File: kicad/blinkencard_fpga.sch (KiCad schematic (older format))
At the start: 19 parts, among them U1 ICE40UP5K-SG48ITR, U2 W25Q64JV

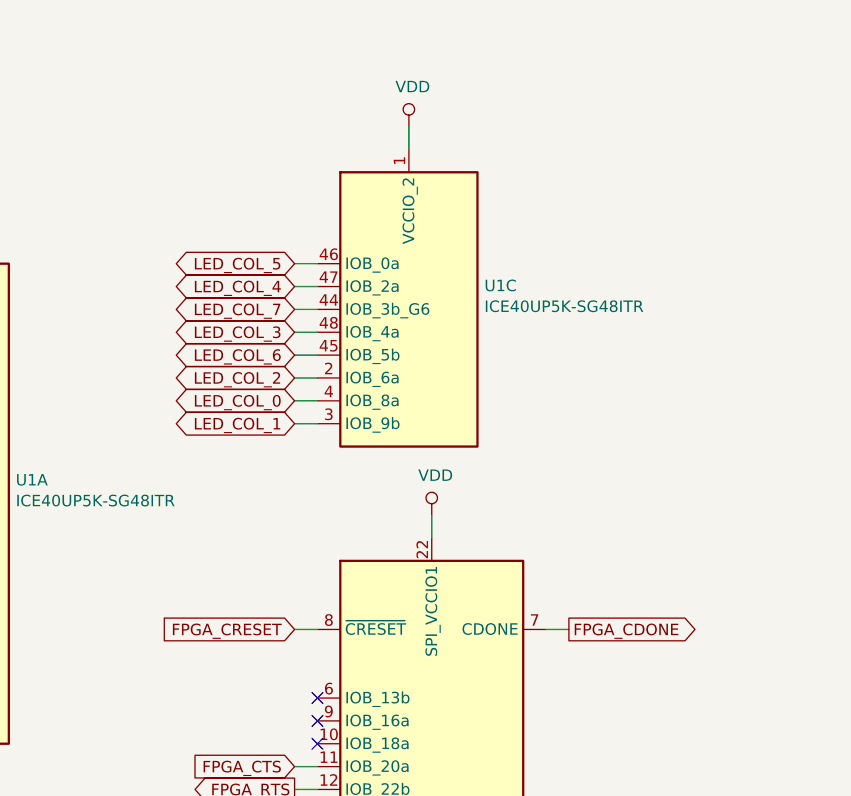
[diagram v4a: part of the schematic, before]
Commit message: Routing complete. DRC passes. Need to fix silk around LEDs and do final check
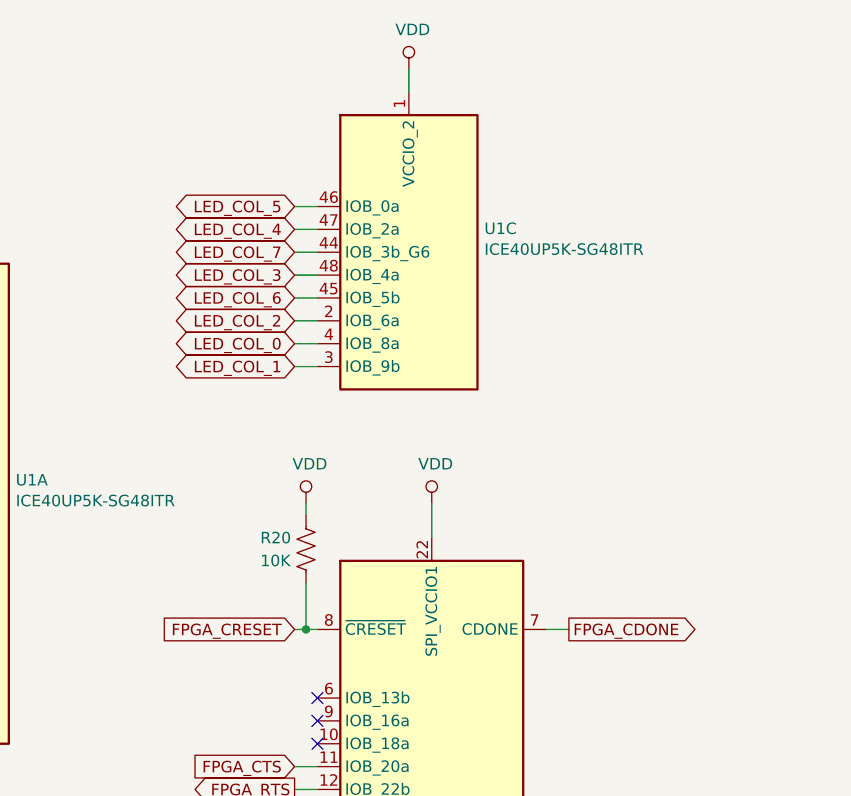
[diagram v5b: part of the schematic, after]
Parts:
- added R20: 10K, Resistor_SMD:R_0603_1608Metric, symbol Device:R_US
- U1: footprint Package_DFN_QFN:QFN-48-1EP_7x7mm_P0.5mm_EP5.6x5.6mm -> Package_DFN_QFN:QFN-48-1EP_7x7mm_P0.5mm_EP5.6x5.6mm_ThermalVias
- U2: footprint Package_SO:SOIC-8_5.23x5.23mm_P1.27mm -> Package_SO:SOIC-8_5.275x5.275mm_P1.27mm
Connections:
- net FPGA_CRESET: now also R20.2
- net VDD: now also R20.1
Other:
- moved on the sheet: U1C
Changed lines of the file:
@@
 F 0 "U1" H 5550 2825 50  0000 C CNN
 F 1 "ICE40UP5K-SG48ITR" H 5550 2734 50  0000 C CNN
-F 2 "Package_DFN_QFN:QFN-48-1EP_7x7mm_P0.5mm_EP5.6x5.6mm" H 5550 2550 50  0001 C CNN
+F 2 "Package_DFN_QFN:QFN-48-1EP_7x7mm_P0.5mm_EP5.6x5.6mm_ThermalVias" H 5550 2550 50  0001 C CNN
 F 3 "http://www.latticesemi.com/Products/FPGAandCPLD/iCE40Ultra" H 5150 4900 50  0001 C CNN
 	2    5550 3900
@@
 L FPGA_Lattice:ICE40UP5K-SG48ITR U1
 U 3 1 5DF0A464
-P 5450 1800
-F 0 "U1" H 5780 1903 50  0000 L CNN
-F 1 "ICE40UP5K-SG48ITR" H 5780 1812 50  0000 L CNN
-F 2 "Package_DFN_QFN:QFN-48-1EP_7x7mm_P0.5mm_EP5.6x5.6mm" H 5450 450 50  0001 C CNN
-F 3 "http://www.latticesemi.com/Products/FPGAandCPLD/iCE40Ultra" H 5050 2800 50  0001 C CNN
-	3    5450 1800
+P 5450 1550
+F 0 "U1" H 5780 1653 50  0000 L CNN
+F 1 "ICE40UP5K-SG48ITR" H 5780 1562 50  0000 L CNN
+F 2 "Package_DFN_QFN:QFN-48-1EP_7x7mm_P0.5mm_EP5.6x5.6mm_ThermalVias" H 5450 200 50  0001 C CNN
+F 3 "http://www.latticesemi.com/Products/FPGAandCPLD/iCE40Ultra" H 5050 2550 50  0001 C CNN
+	3    5450 1550
 	1    0    0    -1
 $EndComp
@@
 F 0 "U1" H 8680 2146 50  0000 L CNN
 F 1 "ICE40UP5K-SG48ITR" H 8680 2055 50  0000 L CNN
-F 2 "Package_DFN_QFN:QFN-48-1EP_7x7mm_P0.5mm_EP5.6x5.6mm" H 8450 750 50  0001 C CNN
+F 2 "Package_DFN_QFN:QFN-48-1EP_7x7mm_P0.5mm_EP5.6x5.6mm_ThermalVias" H 8450 750 50  0001 C CNN
 F 3 "http://www.latticesemi.com/Products/FPGAandCPLD/iCE40Ultra" H 8050 3100 50  0001 C CNN
 	4    8450 2100
@@
 Wire Wire Line
 	3000 3600 2900 3600
-Text GLabel 4950 2300 0    50   3State ~ 0
+Text GLabel 4950 2050 0    50   3State ~ 0
 LED_COL_1
-Text GLabel 4950 2200 0    50   3State ~ 0
+Text GLabel 4950 1950 0    50   3State ~ 0
 LED_COL_0
-Text GLabel 4950 2100 0    50   3State ~ 0
+Text GLabel 4950 1850 0    50   3State ~ 0
 LED_COL_2
-Text GLabel 4950 2000 0    50   3State ~ 0
+Text GLabel 4950 1750 0    50   3State ~ 0
 LED_COL_6
-Text GLabel 4950 1900 0    50   3State ~ 0
+Text GLabel 4950 1650 0    50   3State ~ 0
 LED_COL_3
-Text GLabel 4950 1800 0    50   3State ~ 0
+Text GLabel 4950 1550 0    50   3State ~ 0
 LED_COL_7
-Text GLabel 4950 1700 0    50   3State ~ 0
+Text GLabel 4950 1450 0    50   3State ~ 0
 LED_COL_4
-Text GLabel 4950 1600 0    50   3State ~ 0
+Text GLabel 4950 1350 0    50   3State ~ 0
 LED_COL_5
 Wire Wire Line
-	4950 1600 5050 1600
-Wire Wire Line
-	5050 1700 4950 1700
-Wire Wire Line
-	5050 1800 4950 1800
-Wire Wire Line
-	5050 1900 4950 1900
-Wire Wire Line
-	5050 2000 4950 2000
-Wire Wire Line
-	5050 2100 4950 2100
-Wire Wire Line
-	5050 2200 4950 2200
-Wire Wire Line
-	5050 2300 4950 2300
+	4950 1350 5050 1350
+Wire Wire Line
+	5050 1450 4950 1450
+Wire Wire Line
+	5050 1550 4950 1550
+Wire Wire Line
+	5050 1650 4950 1650
+Wire Wire Line
+	5050 1750 4950 1750
+Wire Wire Line
+	5050 1850 4950 1850
+Wire Wire Line
+	5050 1950 4950 1950
+Wire Wire Line
+	5050 2050 4950 2050
 Text GLabel 4950 4000 0    50   Output ~ 0
 FPGA_TXO
@@
 L power:VDD #PWR08
 U 1 1 5DF1A989
-P 5550 2700
-F 0 "#PWR08" H 5550 2550 50  0001 C CNN
-F 1 "VDD" H 5567 2873 50  0000 C CNN
-F 2 "" H 5550 2700 50  0001 C CNN
-F 3 "" H 5550 2700 50  0001 C CNN
-	1    5550 2700
+P 5550 2650
+F 0 "#PWR08" H 5550 2500 50  0001 C CNN
+F 1 "VDD" H 5567 2823 50  0000 C CNN
+F 2 "" H 5550 2650 50  0001 C CNN
+F 3 "" H 5550 2650 50  0001 C CNN
+	1    5550 2650
 	1    0    0    -1
 $EndComp
@@
 L power:VDD #PWR07
 U 1 1 5DF1B34D
-P 5450 1000
-F 0 "#PWR07" H 5450 850 50  0001 C CNN
-F 1 "VDD" H 5467 1173 50  0000 C CNN
-F 2 "" H 5450 1000 50  0001 C CNN
-F 3 "" H 5450 1000 50  0001 C CNN
-	1    5450 1000
+P 5450 750
+F 0 "#PWR07" H 5450 600 50  0001 C CNN
+F 1 "VDD" H 5467 923 50  0000 C CNN
+F 2 "" H 5450 750 50  0001 C CNN
+F 3 "" H 5450 750 50  0001 C CNN
+	1    5450 750
 	1    0    0    -1
 $EndComp
@@
 	3400 1400 3400 1500
 Wire Wire Line
-	5450 1000 5450 1100
-Wire Wire Line
-	5550 2700 5550 2800
+	5450 750  5450 850
 Text GLabel 2900 2000 0    50   Input ~ 0
 BUTTON_0
@@
 FPGA_CRESET
 Wire Wire Line
-	4950 3200 5050 3200
+	4950 3200 5000 3200
 Wire Wire Line
 	6050 3200 6150 3200
@@
 F 0 "U2" H 2750 6050 50  0000 C CNN
 F 1 "W25Q64JV" H 2850 5950 50  0000 C CNN
-F 2 "Package_SO:SOIC-8_5.23x5.23mm_P1.27mm" H 2450 5650 50  0001 C CNN
+F 2 "Package_SO:SOIC-8_5.275x5.275mm_P1.27mm" H 2450 5650 50  0001 C CNN
 F 3 "https://www.mouser.com/datasheet/2/949/w25q64jv_revj_03272018_plus-1489671.pdf" H 2450 5650 50  0001 C CNN
 	1    2450 5650
@@
 F 0 "U1" H 3730 2653 50  0000 L CNN
 F 1 "ICE40UP5K-SG48ITR" H 3730 2562 50  0000 L CNN
-F 2 "Package_DFN_QFN:QFN-48-1EP_7x7mm_P0.5mm_EP5.6x5.6mm" H 3400 1250 50  0001 C CNN
+F 2 "Package_DFN_QFN:QFN-48-1EP_7x7mm_P0.5mm_EP5.6x5.6mm_ThermalVias" H 3400 1250 50  0001 C CNN
 F 3 "http://www.latticesemi.com/Products/FPGAandCPLD/iCE40Ultra" H 3000 3600 50  0001 C CNN
 	1    3400 2600
@@
 	9950 4000 9450 4000
 Connection ~ 9450 4000
+$Comp
+L Device:R_US R20
+U 1 1 5DD19C71
+P 5000 2850
+F 0 "R20" H 4800 2900 50  0000 L CNN
+F 1 "10K" H 4800 2800 50  0000 L CNN
+F 2 "Resistor_SMD:R_0603_1608Metric" V 5040 2840 50  0001 C CNN
+F 3 "~" H 5000 2850 50  0001 C CNN
+	1    5000 2850
+	1    0    0    -1
+$EndComp
+Wire Wire Line
+	5000 3200 5000 3000
+Connection ~ 5000 3200
+Wire Wire Line
+	5000 3200 5050 3200
+$Comp
+L power:VDD #PWR023
+U 1 1 5DD2024B
+P 5000 2650
+F 0 "#PWR023" H 5000 2500 50  0001 C CNN
+F 1 "VDD" H 5017 2823 50  0000 C CNN
+F 2 "" H 5000 2650 50  0001 C CNN
+F 3 "" H 5000 2650 50  0001 C CNN
+	1    5000 2650
+	1    0    0    -1
+$EndComp
+Wire Wire Line
+	5000 2650 5000 2700
+Wire Wire Line
+	5550 2650 5550 2800
 $EndSCHEMATC

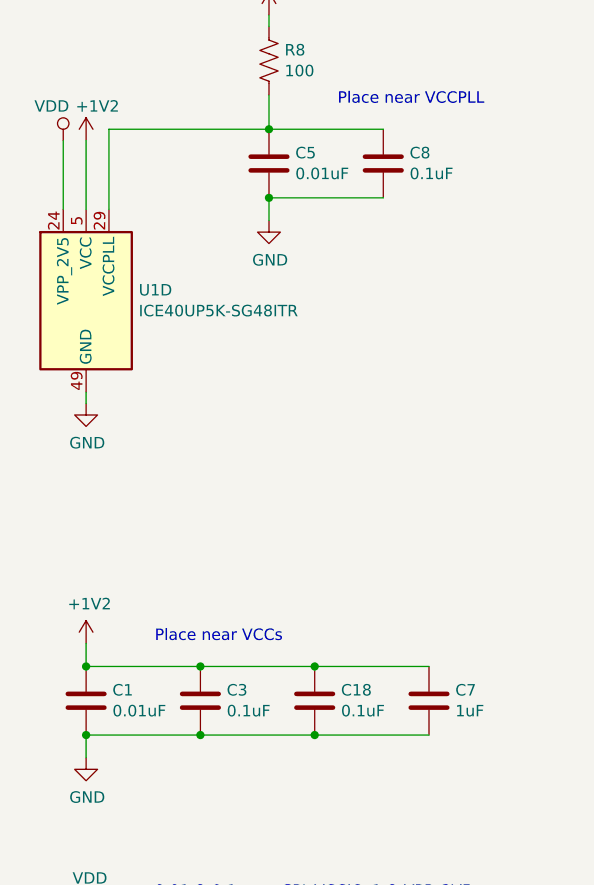
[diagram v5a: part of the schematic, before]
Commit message: Start v1.1 - minor fixes:
- Replace 4.7uF caps with 10uF
- Replace 0.01uF cap in the FPGA VCCPLL filter with 10uF per Lattice's design guideline
- All <1uF caps to 0603 sizes, 1-10uF to 0805
- Make TP? values match between schem and PCB
- Sanitize component values for BOM export consistency
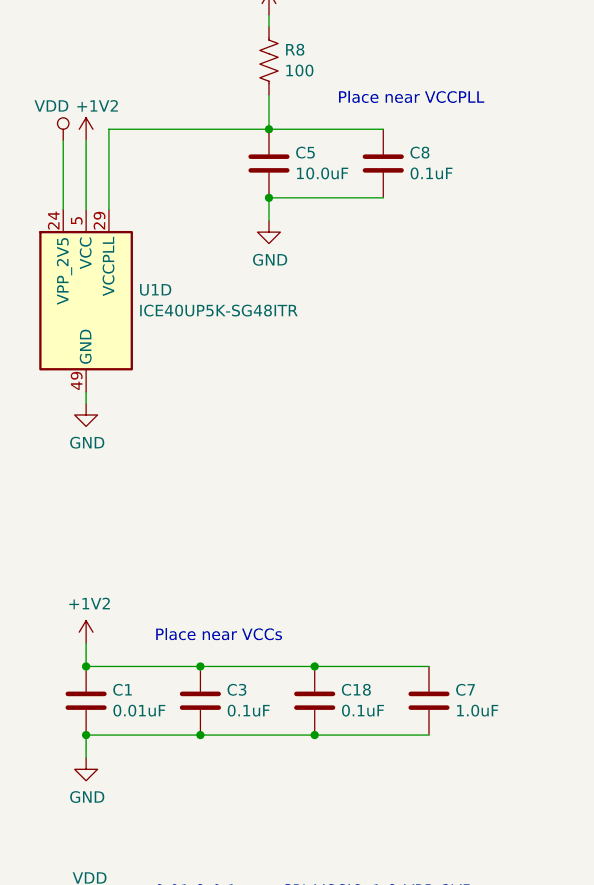
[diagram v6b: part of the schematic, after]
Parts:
- C1, C18, C2, C3, C4, C6, C8, C9: footprint Capacitor_SMD:C_0805_2012Metric -> Capacitor_SMD:C_0603_1608Metric
- C5: value 0.01uF -> 10.0uF
- C7: value 1uF -> 1.0uF
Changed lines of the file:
@@
 F 0 "C1" H 8565 3896 50  0000 L CNN
 F 1 "0.01uF" H 8565 3805 50  0000 L CNN
-F 2 "Capacitor_SMD:C_0805_2012Metric" H 8488 3700 50  0001 C CNN
+F 2 "Capacitor_SMD:C_0603_1608Metric" H 8488 3700 50  0001 C CNN
 F 3 "~" H 8450 3850 50  0001 C CNN
 	1    8450 3850
@@
 F 0 "C3" H 9065 3896 50  0000 L CNN
 F 1 "0.1uF" H 9065 3805 50  0000 L CNN
-F 2 "Capacitor_SMD:C_0805_2012Metric" H 8988 3700 50  0001 C CNN
+F 2 "Capacitor_SMD:C_0603_1608Metric" H 8988 3700 50  0001 C CNN
 F 3 "~" H 8950 3850 50  0001 C CNN
 	1    8950 3850
@@
 P 9950 3850
 F 0 "C7" H 10065 3896 50  0000 L CNN
-F 1 "1uF" H 10065 3805 50  0000 L CNN
+F 1 "1.0uF" H 10065 3805 50  0000 L CNN
 F 2 "Capacitor_SMD:C_0805_2012Metric" H 9988 3700 50  0001 C CNN
 F 3 "~" H 9950 3850 50  0001 C CNN
@@
 	1    0    0    -1
 $EndComp
-$Comp
-L Device:C C8
-U 1 1 5DD47433
-P 9750 1500
-F 0 "C8" H 9865 1546 50  0000 L CNN
-F 1 "0.1uF" H 9865 1455 50  0000 L CNN
-F 2 "Capacitor_SMD:C_0805_2012Metric" H 9788 1350 50  0001 C CNN
-F 3 "~" H 9750 1500 50  0001 C CNN
-	1    9750 1500
-	1    0    0    -1
-$EndComp
-$Comp
-L Device:C C5
-U 1 1 5DD47429
-P 9250 1500
-F 0 "C5" H 9365 1546 50  0000 L CNN
-F 1 "0.01uF" H 9365 1455 50  0000 L CNN
-F 2 "Capacitor_SMD:C_0805_2012Metric" H 9288 1350 50  0001 C CNN
-F 3 "~" H 9250 1500 50  0001 C CNN
-	1    9250 1500
-	1    0    0    -1
-$EndComp
 Wire Wire Line
 	8550 1700 8550 1350
@@
 F 0 "C2" H 8565 5096 50  0000 L CNN
 F 1 "0.01uF" H 8565 5005 50  0000 L CNN
-F 2 "Capacitor_SMD:C_0805_2012Metric" H 8488 4900 50  0001 C CNN
+F 2 "Capacitor_SMD:C_0603_1608Metric" H 8488 4900 50  0001 C CNN
 F 3 "~" H 8450 5050 50  0001 C CNN
 	1    8450 5050
@@
 F 0 "C4" H 9065 5096 50  0000 L CNN
 F 1 "0.1uF" H 9065 5005 50  0000 L CNN
-F 2 "Capacitor_SMD:C_0805_2012Metric" H 8988 4900 50  0001 C CNN
+F 2 "Capacitor_SMD:C_0603_1608Metric" H 8988 4900 50  0001 C CNN
 F 3 "~" H 8950 5050 50  0001 C CNN
 	1    8950 5050
@@
 F 0 "C9" H 10015 5096 50  0000 L CNN
 F 1 "0.1uF" H 10015 5005 50  0000 L CNN
-F 2 "Capacitor_SMD:C_0805_2012Metric" H 9938 4900 50  0001 C CNN
+F 2 "Capacitor_SMD:C_0603_1608Metric" H 9938 4900 50  0001 C CNN
 F 3 "~" H 9900 5050 50  0001 C CNN
 	1    9900 5050
@@
 F 0 "C6" H 9515 5096 50  0000 L CNN
 F 1 "0.1uF" H 9515 5005 50  0000 L CNN
-F 2 "Capacitor_SMD:C_0805_2012Metric" H 9438 4900 50  0001 C CNN
+F 2 "Capacitor_SMD:C_0603_1608Metric" H 9438 4900 50  0001 C CNN
 F 3 "~" H 9400 5050 50  0001 C CNN
 	1    9400 5050
@@
 F 0 "C18" H 9565 3896 50  0000 L CNN
 F 1 "0.1uF" H 9565 3805 50  0000 L CNN
-F 2 "Capacitor_SMD:C_0805_2012Metric" H 9488 3700 50  0001 C CNN
+F 2 "Capacitor_SMD:C_0603_1608Metric" H 9488 3700 50  0001 C CNN
 F 3 "~" H 9450 3850 50  0001 C CNN
 	1    9450 3850
@@
 Wire Wire Line
 	5550 2650 5550 2800
+$Comp
+L Device:C C8
+U 1 1 5DD47433
+P 9750 1500
+F 0 "C8" H 9865 1546 50  0000 L CNN
+F 1 "0.1uF" H 9865 1455 50  0000 L CNN
+F 2 "Capacitor_SMD:C_0603_1608Metric" H 9788 1350 50  0001 C CNN
+F 3 "~" H 9750 1500 50  0001 C CNN
+	1    9750 1500
+	1    0    0    -1
+$EndComp
+$Comp
+L Device:C C5
+U 1 1 5DD47429
+P 9250 1500
+F 0 "C5" H 9365 1546 50  0000 L CNN
+F 1 "10.0uF" H 9365 1455 50  0000 L CNN
+F 2 "Capacitor_SMD:C_0805_2012Metric" H 9288 1350 50  0001 C CNN
+F 3 "~" H 9250 1500 50  0001 C CNN
+	1    9250 1500
+	1    0    0    -1
+$EndComp
 $EndSCHEMATC

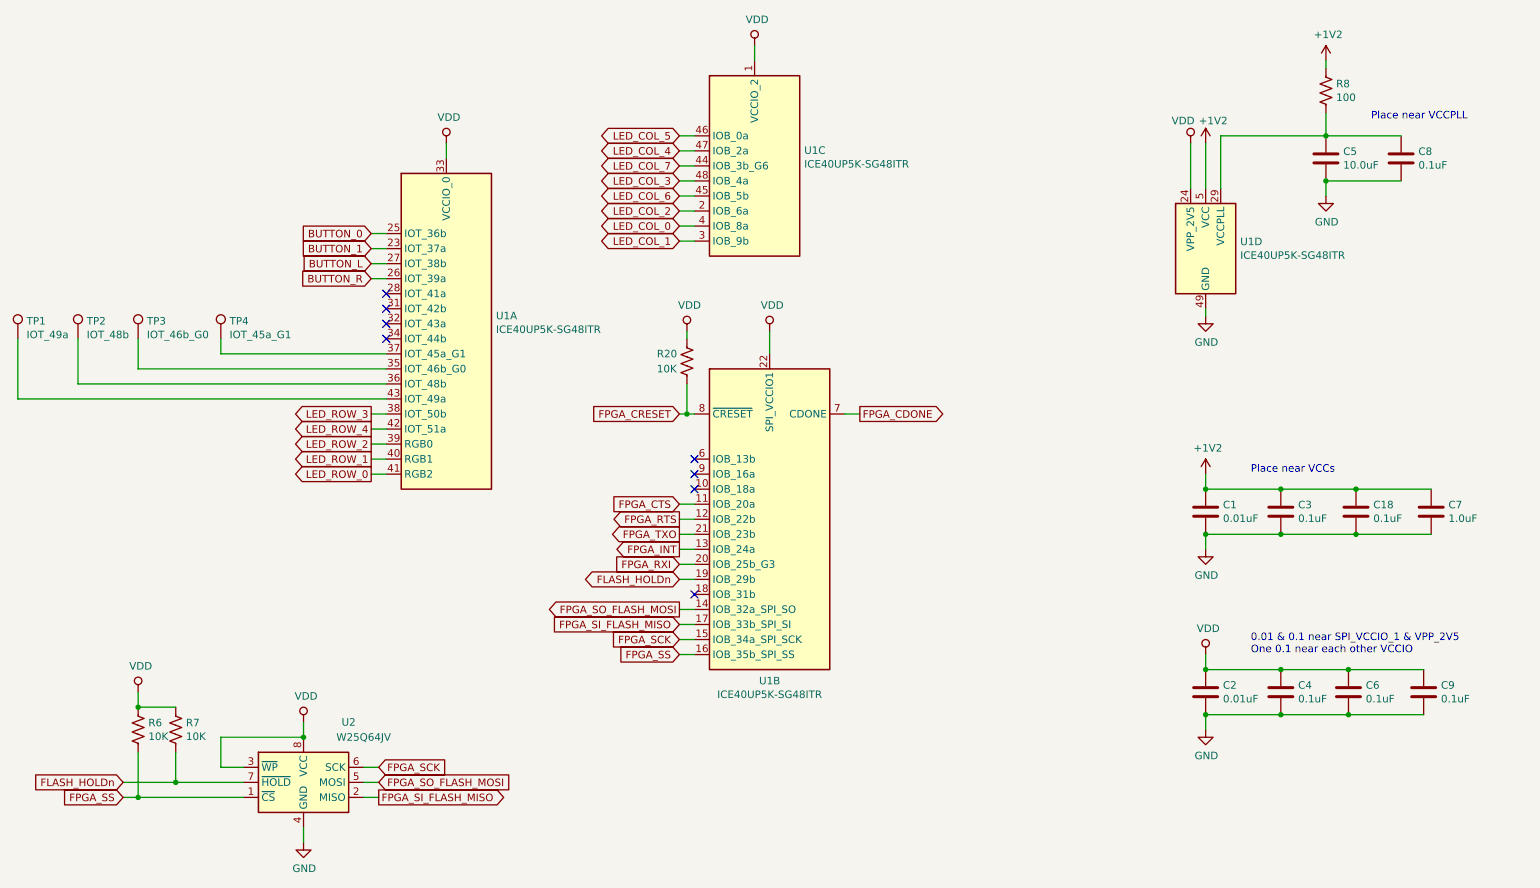
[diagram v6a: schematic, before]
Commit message: Start v2.0 - change USB-UART to ESP32 and bugfixes
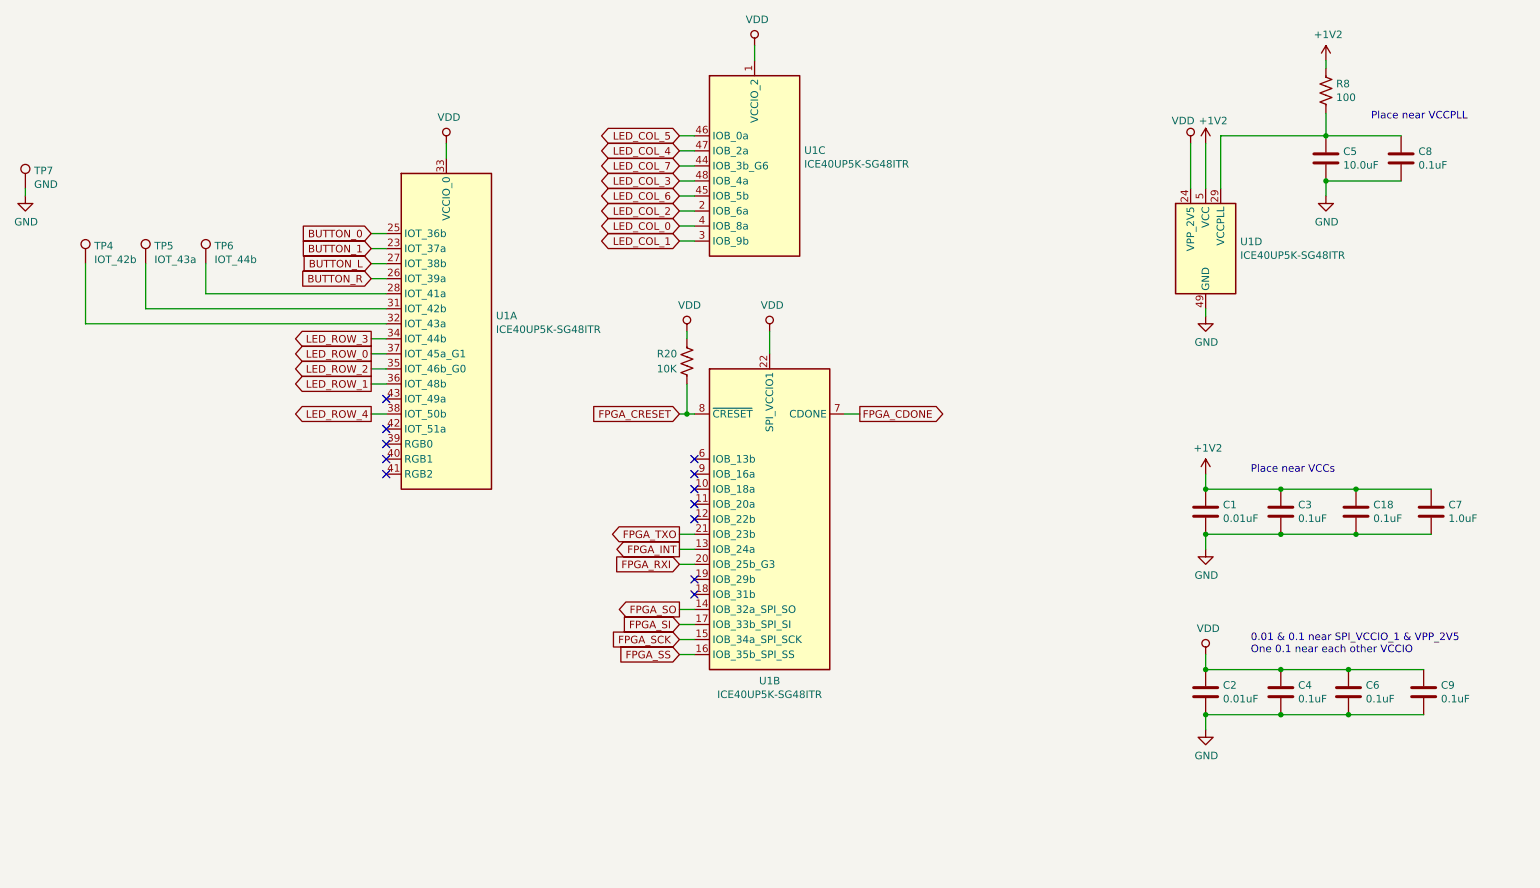
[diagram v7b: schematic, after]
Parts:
- removed R6, R7: 10K, Resistor_SMD:R_0603_1608Metric, symbol Device:R_US
- removed TP1: IOT_49a, TestPoint:TestPoint_Pad_D1.5mm, symbol Connector:TestPoint
- removed TP2: IOT_48b, TestPoint:TestPoint_Pad_D1.5mm, symbol Connector:TestPoint
- removed TP3: IOT_46b_G0, TestPoint:TestPoint_Pad_D1.5mm, symbol Connector:TestPoint
- removed U2: W25Q64JV, Package_SO:SOIC-8_5.275x5.275mm_P1.27mm, symbol Memory_EEPROM:25LCxxx
- added TP5: IOT_43a, TestPoint:TestPoint_Pad_D1.5mm, symbol Connector:TestPoint
- added TP6: IOT_44b, TestPoint:TestPoint_Pad_D1.5mm, symbol Connector:TestPoint
- added TP7: GND, TestPoint:TestPoint_Pad_D1.5mm, symbol Connector:TestPoint
- TP4: value IOT_45a_G1 -> IOT_42b
- U1: footprint Package_DFN_QFN:QFN-48-1EP_7x7mm_P0.5mm_EP5.6x5.6mm_ThermalVias -> Package_DFN_QFN:QFN-48-1EP_7x7mm_P0.5mm_EP5.15x5.15mm_ThermalVias
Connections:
- net GND: now also TP7.1
- net LED_ROW_0: now also U1.37 (IOT_45a_G1); no longer U1.41 (RGB2)
- net LED_ROW_1: now also U1.36 (IOT_48b); no longer U1.40 (RGB1)
- net LED_ROW_2: now also U1.35 (IOT_46b_G0); no longer U1.39 (RGB0)
- net LED_ROW_3: now also U1.34 (IOT_44b); no longer U1.38 (IOT_50b)
- net LED_ROW_4: now also U1.38 (IOT_50b); no longer U1.42 (IOT_51a)
- net at TP4.1: now also U1.32 (IOT_43a); no longer U1.37 (IOT_45a_G1)
- net at U1.28 (IOT_41a): now also TP6.1
- net at U1.31 (IOT_42b): now also TP5.1
- net FLASH_HOLDn: no longer names the net of U1.19 (IOB_29b)
- net FPGA_CTS: no longer names the net of U1.11 (IOB_20a)
- net FPGA_RTS: no longer names the net of U1.12 (IOB_22b)
- net FPGA_SI_FLASH_MISO renamed FPGA_SI
- net FPGA_SO_FLASH_MOSI renamed FPGA_SO
- no-connect marks 8 -> 12

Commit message: v2.0 release - clean silk, add order number placeholder for JLCPCB, add MFG PN in components for BOM, add BOM, add STEP, generate fab outputs
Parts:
- C1, C2:  mfg_part (none) -> CL21B103KBANNNC
- C18, C3, C4, C6, C8, C9:  mfg_part (none) -> CL10F104ZO8NNNC
- C5:  mfg_part (none) -> CL21A106KQCLRNC
- C7:  mfg_part (none) -> CL21B105KOFNNNG
- R20:  mfg_part (none) -> RC0603JR-0710KL
- R8:  mfg_part (none) -> RC0603JR-07100RL
- TP4, TP5, TP6, TP7:  mfg_part (none) -> NP
- U1:  mfg_part (none) -> ICE40UP5K-SG48I
